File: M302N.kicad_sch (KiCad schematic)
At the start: 3 parts, among them J1 Analog, J2 Digital, U101 W5500

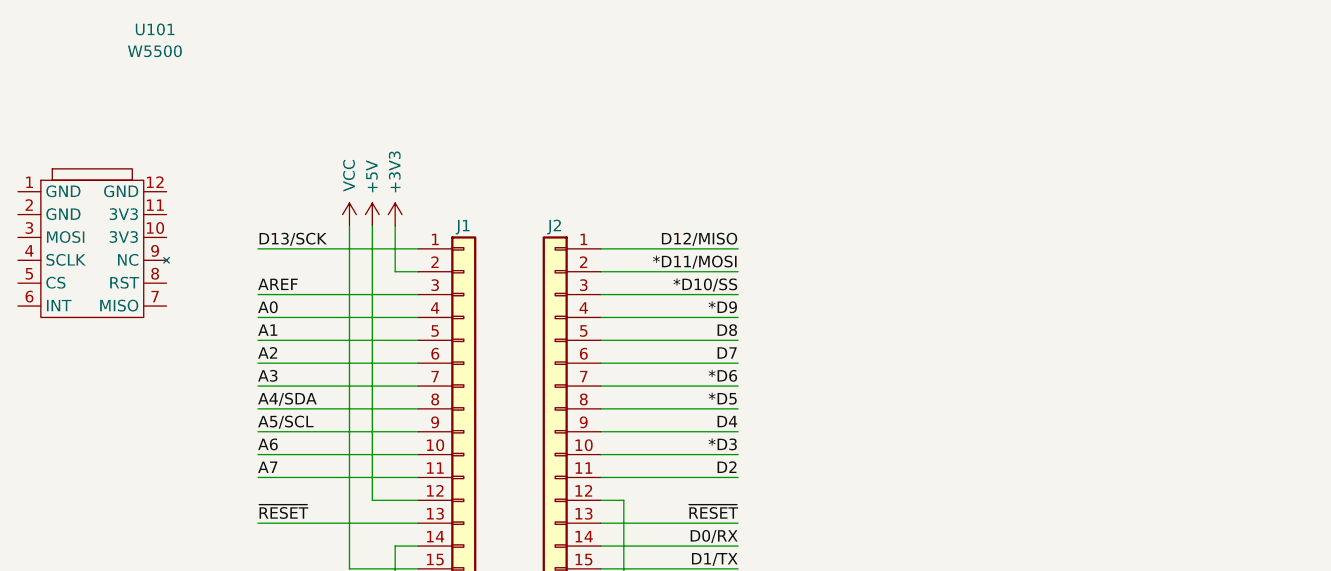
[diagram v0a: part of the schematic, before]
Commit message: W5500新しいシンボルとフットパターン
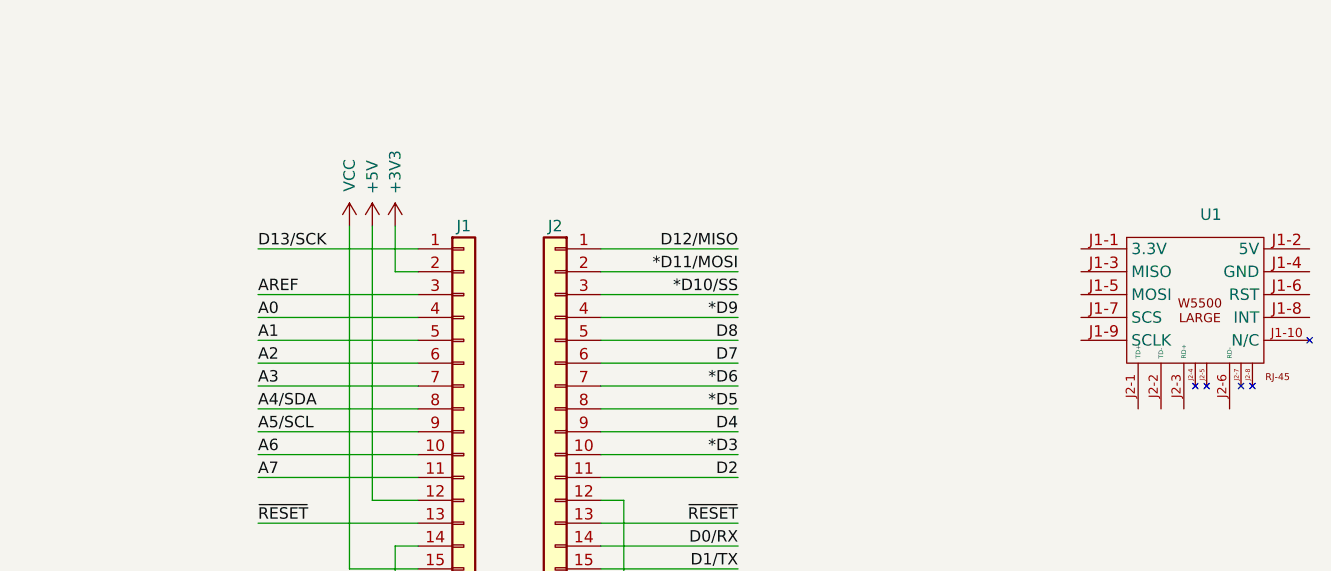
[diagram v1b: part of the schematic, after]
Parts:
- removed U101: W5500, symbol holly:W5500
- added U1: W5500, HOLLY2:W5500LARGE, symbol holly:W5500LARGE
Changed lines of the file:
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@@
 	(label "D4"
 		(at 154.94 88.9 180)
-		(fields_autoplaced yes)
 		(effects
 			(font
@@
 	(label "*D5"
 		(at 154.94 86.36 180)
-		(fields_autoplaced yes)
 		(effects
 			(font
@@
 	(label "A2"
 		(at 101.6 81.28 0)
-		(fields_autoplaced yes)
 		(effects
 			(font
@@
 	(label "D7"
 		(at 154.94 81.28 180)
-		(fields_autoplaced yes)
 		(effects
 			(font
@@
 	(label "D13{slash}SCK"
 		(at 101.6 68.58 0)
-		(fields_autoplaced yes)
 		(effects
 			(font
@@
 	(label "A7"
 		(at 101.6 93.98 0)
-		(fields_autoplaced yes)
 		(effects
 			(font
@@
 	(label "*D6"
 		(at 154.94 83.82 180)
-		(fields_autoplaced yes)
 		(effects
 			(font
@@
 	(label "*D11{slash}MOSI"
 		(at 154.94 71.12 180)
-		(fields_autoplaced yes)
 		(effects
 			(font
@@
 	(label "A1"
 		(at 101.6 78.74 0)
-		(fields_autoplaced yes)
 		(effects
 			(font
@@
 	(label "A4{slash}SDA"
 		(at 101.6 86.36 0)
-		(fields_autoplaced yes)
 		(effects
 			(font
@@
 	(label "A5{slash}SCL"
 		(at 101.6 88.9 0)
-		(fields_autoplaced yes)
 		(effects
 			(font
@@
 	(label "A3"
 		(at 101.6 83.82 0)
-		(fields_autoplaced yes)
 		(effects
 			(font
@@
 	(label "~{RESET}"
 		(at 154.94 99.06 180)
-		(fields_autoplaced yes)
 		(effects
 			(font
@@
 	(label "~{RESET}"
 		(at 101.6 99.06 0)
-		(fields_autoplaced yes)
 		(effects
 			(font
@@
 	(label "A6"
 		(at 101.6 91.44 0)
-		(fields_autoplaced yes)
 		(effects
 			(font
@@
 	(label "A0"
 		(at 101.6 76.2 0)
-		(fields_autoplaced yes)
 		(effects
 			(font
@@
 	(label "*D9"
 		(at 154.94 76.2 180)
-		(fields_autoplaced yes)
 		(effects
 			(font
@@
 	(label "*D3"
 		(at 154.94 91.44 180)
-		(fields_autoplaced yes)
 		(effects
 			(font
@@
 	(label "D2"
 		(at 154.94 93.98 180)
-		(fields_autoplaced yes)
 		(effects
 			(font
@@
 	(label "D8"
 		(at 154.94 78.74 180)
-		(fields_autoplaced yes)
 		(effects
 			(font
@@
 	(label "D1{slash}TX"
 		(at 154.94 104.14 180)
-		(fields_autoplaced yes)
 		(effects
 			(font
@@
 	(label "D0{slash}RX"
 		(at 154.94 101.6 180)
-		(fields_autoplaced yes)
 		(effects
 			(font
@@
 	(label "AREF"
 		(at 101.6 73.66 0)
-		(fields_autoplaced yes)
 		(effects
 			(font
@@
 	(label "*D10{slash}SS"
 		(at 154.94 73.66 180)
-		(fields_autoplaced yes)
 		(effects
 			(font
@@
 	(label "D12{slash}MISO"
 		(at 154.94 68.58 180)
-		(fields_autoplaced yes)
 		(effects
 			(font
@@
 	)
 	(symbol
-		(lib_id "holly:W5500")
-		(at 82.55 68.58 0)
-		(unit 1)
-		(exclude_from_sim no)
-		(in_bom yes)
-		(on_board yes)
-		(dnp no)
-		(fields_autoplaced yes)
-		(property "Reference" "U101"
-			(at 90.17 44.2425 0)
-			(effects
-				(font
-					(size 1.27 1.27)
-				)
-			)
-		)
-		(property "Value" "W5500"
-			(at 90.17 46.6668 0)
-			(effects
-				(font
-					(size 1.27 1.27)
-				)
-			)
-		)
-		(property "Footprint" ""
-			(at 82.55 68.58 0)
-			(effects
-				(font
-					(size 1.27 1.27)
-				)
-				(hide yes)
-			)
-		)
-		(property "Datasheet" ""
-			(at 81.28 78.74 0)
-			(effects
-				(font
-					(size 1.27 1.27)
-				)
-				(hide yes)
-			)
-		)
-		(property "Description" "Tzt smart electronics USR-ES1"
-			(at 82.55 68.58 0)
-			(effects
-				(font
-					(size 1.27 1.27)
-				)
-				(hide yes)
-			)
-		)
-		(pin "5"
-		)
-		(pin "7"
-		)
-		(pin "8"
-		)
-		(pin "1"
-		)
-		(pin "6"
-		)
-		(pin "10"
-		)
-		(pin "11"
-		)
-		(pin "12"
-		)
-		(pin "2"
-		)
-		(pin "3"
-		)
-		(pin "4"
-		)
-		(pin "9"
-		)
-		(instances
-			(project ""
-				(path "/0d35483a-0b12-46cc-b9f2-896fd6831779"
-					(reference "U101")
-					(unit 1)
-				)
-			)
-		)
-	)
-	(symbol
 		(lib_id "power:GND")
 		(at 142.24 106.68 0)
@@
 					(unit 1)
 				)
+			)
+		)
+	)
+	(symbol
+		(lib_id "holly:W5500LARGE")
+		(at 205.74 66.04 0)
+		(unit 1)
+		(exclude_from_sim no)
+		(in_bom yes)
+		(on_board yes)
+		(dnp no)
+		(fields_autoplaced yes)
+		(property "Reference" "U1"
+			(at 207.4697 64.77 0)
+			(effects
+				(font
+					(size 1.27 1.27)
+				)
+			)
+		)
+		(property "Value" "W5500"
+			(at 205.74 66.04 0)
+			(effects
+				(font
+					(size 1.27 1.27)
+				)
+				(hide yes)
+			)
+		)
+		(property "Footprint" "HOLLY2:W5500LARGE"
+			(at 205.74 66.04 0)
+			(effects
+				(font
+					(size 1.27 1.27)
+				)
+				(hide yes)
+			)
+		)
+		(property "Datasheet" ""
+			(at 205.74 66.04 0)
+			(effects
+				(font
+					(size 1.27 1.27)
+				)
+				(hide yes)
+			)
+		)
+		(property "Description" ""
+			(at 205.74 66.04 0)
+			(effects
+				(font
+					(size 1.27 1.27)
+				)
+				(hide yes)
+			)
+		)
+		(pin "J2-8"
+		)
+		(pin "J1-9"
+		)
+		(pin "J2-4"
+		)
+		(pin "J2-7"
+		)
+		(pin "J1-3"
+		)
+		(pin "J1-4"
+		)
+		(pin "J1-5"
+		)
+		(pin "J1-6"
+		)
+		(pin "J1-2"
+		)
+		(pin "J1-10"
+		)
+		(pin "J1-1"
+		)
+		(pin "J2-1"
+		)
+		(pin "J2-5"
+		)
+		(pin "J2-2"
+		)
+		(pin "J1-8"
+		)
+		(pin "J2-6"
+		)
+		(pin "J1-7"
+		)
+		(pin "J2-3"
+		)
+		(instances
+			(project ""
+				(path "/0d35483a-0b12-46cc-b9f2-896fd6831779"
+					(reference "U1")
+					(unit 1)
+				)

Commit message: 途中
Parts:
- added C101: 0.1uF, symbol Device:C_Small
- added D101: 1N4001, Diode_THT:D_DO-41_SOD81_P10.16mm_Horizontal, symbol Diode:1N4001
- added FL101: 0.1uF DDS1, HOLLY:DSS1, symbol 001-rescue:EMI_Filter_LCL-Device
- added J101: I2C-1, Connector_JST:JST_XH_S4B-XH-A_1x04_P2.50mm_Horizontal, symbol Connector_Generic:Conn_01x04
- added J102: I2C-2, Connector_JST:JST_XH_S4B-XH-A_1x04_P2.50mm_Horizontal, symbol Connector_Generic:Conn_01x04
- added J103: ADC_IN, Connector_JST:JST_XH_S3B-XH-A_1x03_P2.50mm_Horizontal, symbol Connector_Generic:Conn_01x03
- added J104: RJ45, symbol Connector:RJ45
- added J105: DC12V FAN, symbol Connector_Generic:Conn_01x02
- added R101: 10k, symbol Device:R_US
- added R102: TNR10V471K, symbol Device:R_Variable_US
- added SW101: SW_Reed, symbol Switch:SW_Reed
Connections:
- net *D10/SS: now also U1.J1-7 (SCS)
- net *D11/MOSI: now also U1.J1-5 (MOSI)
- net +5V: now also U1.J1-2 (5V), J101.2 (Pin_2), J102.2 (Pin_2), J103.3 (Pin_3), R101.1
- net A4/SDA: now also J101.3 (Pin_3), J102.3 (Pin_3)
- net A5/SCL: now also J101.4 (Pin_4), J102.4 (Pin_4)
- net A7: now also J103.2 (Pin_2)
- net D12/MISO: now also U1.J1-3 (MISO)
- net D13/SCK: now also U1.J1-9 (SCLK)
- net GND: now also U1.J1-4 (GND), C101.2, D101.2 (A), FL101.2, J101.1 (Pin_1), J102.1 (Pin_1), J103.1 (Pin_1), J104.7, J104.8, J105.1 (Pin_1), R102.2, SW101.1
- net ~{RESET}: now also U1.J1-6 (RST), R101.2, SW101.2
- net at U1.J2-1 (TD+): now also J104.1
- net at U1.J2-2 (TD-): now also J104.2
- net at U1.J2-3 (RD+): now also J104.3
- net at U1.J2-6 (RD-): now also J104.6
- new net +12V: C101.1, D101.1 (K), FL101.3, J104.4, J104.5, J105.2 (Pin_2), R102.1
- no-connect marks 0 -> 2
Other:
- note added: "NJU7223"
- company: (none) -> YS-Lab Masafumi Horimoto
- title: (none) -> M302N
- moved on the sheet: U1

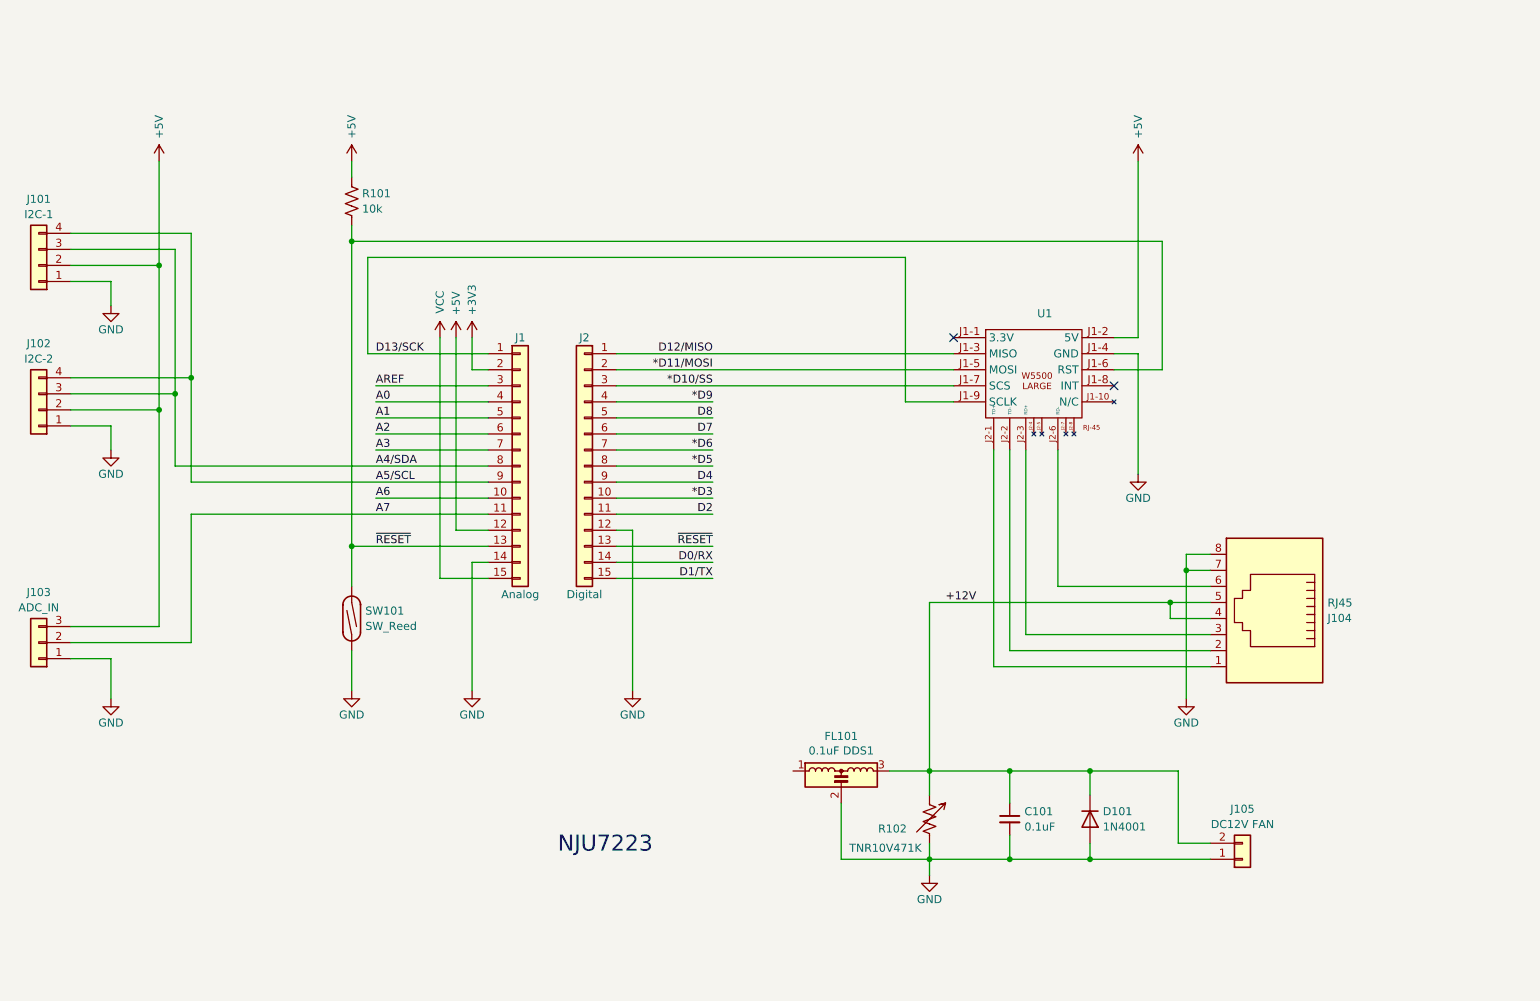
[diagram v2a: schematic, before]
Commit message: W5500との接続はソケット
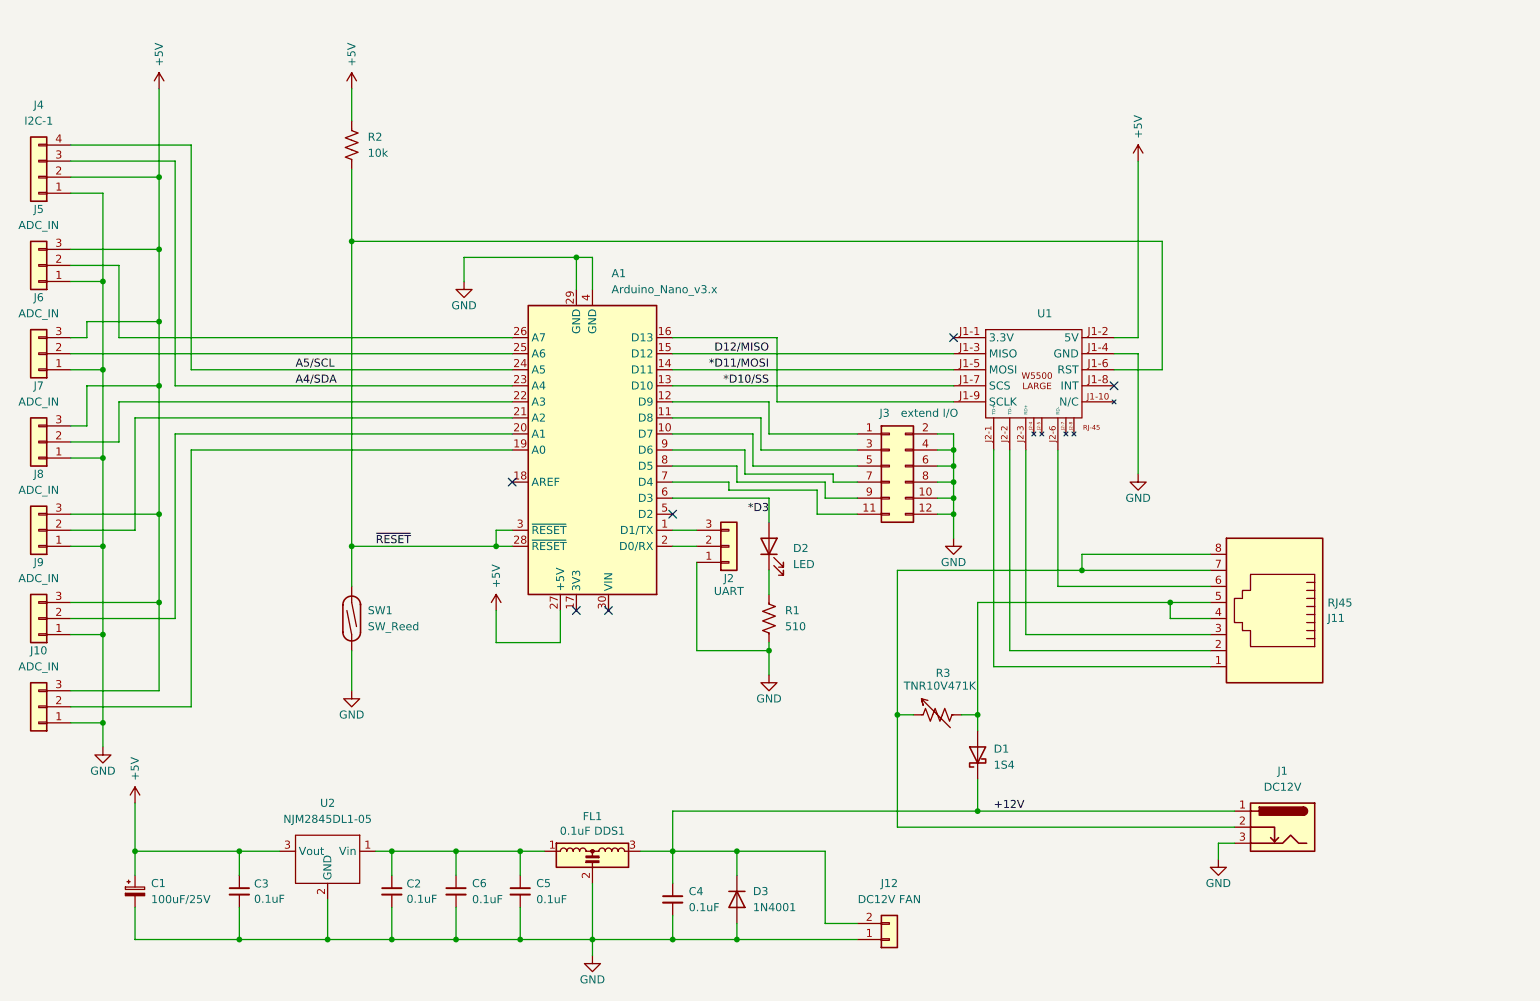
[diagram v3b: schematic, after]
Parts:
- removed J1: Analog, Connector_PinHeader_2.54mm:PinHeader_1x15_P2.54mm_Vertical, symbol Connector_Generic:Conn_01x15
- removed J102: I2C-2, Connector_JST:JST_XH_S4B-XH-A_1x04_P2.50mm_Horizontal, symbol Connector_Generic:Conn_01x04
- removed J2: Digital, Connector_PinHeader_2.54mm:PinHeader_1x15_P2.54mm_Vertical, symbol Connector_Generic:Conn_01x15
- added A1: Arduino_Nano_v3.x, Arduino:Arduino_Nano, symbol MCU_Module:Arduino_Nano_v3.x
- added C1: 100uF/25V, Capacitor_THT:C_Radial_D5.0mm_H11.0mm_P2.00mm, symbol Device:C_Polarized_Small
- added C2, C3, C5, C6: 0.1uF, Capacitor_THT:C_Disc_D4.3mm_W1.9mm_P5.00mm, symbol Device:C_Small
- added D1: 1S4, Resistor_THT:R_Axial_DIN0204_L3.6mm_D1.6mm_P5.08mm_Horizontal, symbol Device:D_Schottky
- added D2: LED, LED_THT:LED_D3.0mm, symbol Device:LED
- added J1: DC12V, Connector_BarrelJack:BarrelJack_GCT_DCJ200-10-A_Horizontal, symbol Connector:Barrel_Jack_Switch_Pin3Ring
- added J2: UART, Connector_PinHeader_2.54mm:PinHeader_1x03_P2.54mm_Vertical, symbol Connector_Generic:Conn_01x03
- added J3: extend I/O, Connector_PinHeader_2.54mm:PinHeader_2x06_P2.54mm_Vertical, symbol Connector_Generic:Conn_02x06_Odd_Even
- added J5, J6, J7, J8, J9: ADC_IN, Connector_JST:JST_XH_S3B-XH-A_1x03_P2.50mm_Horizontal, symbol Connector_Generic:Conn_01x03
- added R1: 510, Resistor_THT:R_Axial_DIN0207_L6.3mm_D2.5mm_P7.62mm_Horizontal, symbol Device:R_US
- added U2: NJM2845DL1-05, HOLLY2:NJM2845, symbol holly:NJM2845DL1
- C4: renamed from C101; footprint (none) -> Capacitor_THT:C_Disc_D4.3mm_W1.9mm_P5.00mm
- FL1: renamed from FL101; footprint HOLLY:DSS1 -> HOLLY2:DSS1
- J11: renamed from J104; footprint (none) -> HOLLY2:RJ45_Neltron_7810-8P8C
- J12: renamed from J105; footprint (none) -> Connector_JST:JST_XH_S2B-XH-A_1x02_P2.50mm_Horizontal
- R2: renamed from R101; footprint (none) -> Resistor_THT:R_Axial_DIN0207_L6.3mm_D2.5mm_P7.62mm_Horizontal
- renumbered D101 to D3, J103 to J10, J101 to J4, R102 to R3, SW101 to SW1
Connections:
- net *D10/SS: now also A1.13 (D10)
- net *D11/MOSI: now also A1.14 (D11)
- net *D3: now also A1.6 (D3), D2.2 (A)
- net +12V: now also D1.1 (K), J1.1; no longer J11.4, J11.5, R3.1
- net +5V: now also A1.27 (+5V), C1.1, C3.1, J5.3 (Pin_3), J6.3 (Pin_3), J7.3 (Pin_3), J8.3 (Pin_3), J9.3 (Pin_3), U2.3 (Vout)
- net A4/SDA: now also A1.23 (A4)
- net A5/SCL: now also A1.24 (A5)
- net D12/MISO: now also A1.15 (D12)
- net GND: now also A1.29 (GND), A1.4 (GND), C1.2, C2.2, C3.2, C5.2, C6.2, J1.3, J2.1 (Pin_1), J3.10 (Pin_10), J3.12 (Pin_12), J3.2 (Pin_2), J3.4 (Pin_4), J3.6 (Pin_6), J3.8 (Pin_8), J5.1 (Pin_1), J6.1 (Pin_1), J7.1 (Pin_1), J8.1 (Pin_1), J9.1 (Pin_1), R1.2, U2.2 (GND); no longer J11.7, J11.8, R3.2
- net ~{RESET}: now also A1.28 (~{RESET}), A1.3 (~{RESET})
- net at FL1.1: now also C2.1, C5.1, C6.1, U2.1 (Vin)
- net A7: no longer names the net of J10.2 (Pin_2)
- net A7: now also A1.19 (A0)
- net D13/SCK: no longer names the net of U1.J1-9 (SCLK)
- net D13/SCK: now also A1.16 (D13)
- new net: D2.1 (K), R1.1
- new net: D1.2 (A), J11.4, J11.5, R3.2
- new net: A1.26 (A7), J5.2 (Pin_2)
- new net: A1.22 (A3), J7.2 (Pin_2)
- new net: J1.2, J11.7, J11.8, R3.1
- new net: A1.2 (D0/RX), J2.2 (Pin_2)
- new net: A1.1 (D1/TX), J2.3 (Pin_3)
- new net: A1.12 (D9), J3.1 (Pin_1)
- new net: A1.7 (D4), J3.11 (Pin_11)
- new net: A1.11 (D8), J3.3 (Pin_3)
- new net: A1.10 (D7), J3.5 (Pin_5)
- new net: A1.9 (D6), J3.7 (Pin_7)
- new net: A1.8 (D5), J3.9 (Pin_9)
- new net: A1.25 (A6), J6.2 (Pin_2)
- new net: A1.21 (A2), J8.2 (Pin_2)
- new net: A1.20 (A1), J9.2 (Pin_2)
- no-connect marks 2 -> 6
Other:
- note removed: "NJU7223"
- moved on the sheet: C4, D3, FL1, J10, J12, J4, R2, R3

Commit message: PCB設計途中
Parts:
- added J13, J14: Conn_01x05_Socket, Connector_PinSocket_2.54mm:PinSocket_1x05_P2.54mm_Vertical, symbol Connector:Conn_01x05_Socket
- added J15, J16: Conn_01x05_Pin, symbol Connector:Conn_01x05_Pin
- added J17: Conn_01x08_Pin, symbol Connector:Conn_01x08_Pin
- added J18, J19: Conn_01x04_Socket, Connector_PinSocket_2.54mm:PinSocket_1x04_P2.54mm_Vertical, symbol Connector:Conn_01x04_Socket
- A1: footprint Arduino:Arduino_Nano -> Module:Arduino_Nano
- SW1: footprint (none) -> HOLLY:REED_SW
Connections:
- net *D10/SS: no longer A1.13 (D10), U1.J1-7 (SCS)
- net *D11/MOSI: no longer A1.14 (D11), U1.J1-5 (MOSI)
- net +5V: now also J14.1 (Pin_1); no longer U1.J1-2 (5V)
- net D12/MISO: no longer A1.15 (D12), U1.J1-3 (MISO)
- net GND: now also J14.2 (Pin_2); no longer U1.J1-4 (GND)
- net ~{RESET}: now also J14.3 (Pin_3); no longer U1.J1-6 (RST)
- net at U1.J2-1 (TD+): now also J17.1 (Pin_1); no longer J11.1
- net at U1.J2-2 (TD-): now also J17.2 (Pin_2); no longer J11.2
- net at U1.J2-3 (RD+): now also J17.3 (Pin_3); no longer J11.3
- net at U1.J2-6 (RD-): now also J17.6 (Pin_6); no longer J11.6
- net at A1.16 (D13): now also J13.5 (Pin_5); no longer U1.J1-9 (SCLK)
- new net: A1.15 (D12), J13.2 (Pin_2)
- new net: A1.14 (D11), J13.3 (Pin_3)
- new net: A1.13 (D10), J13.4 (Pin_4)
- new net: J16.1 (Pin_1), U1.J1-2 (5V)
- new net: J16.2 (Pin_2), U1.J1-4 (GND)
- new net: J16.3 (Pin_3), U1.J1-6 (RST)
- new net: J11.6, J19.2 (Pin_2)
- new net: J11.1, J18.1 (Pin_1)
- new net: J11.2, J18.2 (Pin_2)
- new net: J11.3, J18.3 (Pin_3)
- new net: J15.2 (Pin_2), U1.J1-3 (MISO)
- new net: J15.3 (Pin_3), U1.J1-5 (MOSI)
- new net: J15.4 (Pin_4), U1.J1-7 (SCS)
- new net: J15.5 (Pin_5), U1.J1-9 (SCLK)
- no-connect marks 6 -> 20
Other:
- moved on the sheet: J11, U1

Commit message: PCB設計とRJ45モジュラー
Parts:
- J10, J6, J7, J8, J9: footprint Connector_JST:JST_XH_S3B-XH-A_1x03_P2.50mm_Horizontal -> Connector_JST:JST_XH_B3B-XH-A_1x03_P2.50mm_Vertical
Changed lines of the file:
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@@
 			)
 		)
-		(property "Footprint" "Connector_JST:JST_XH_S3B-XH-A_1x03_P2.50mm_Horizontal"
+		(property "Footprint" "Connector_JST:JST_XH_B3B-XH-A_1x03_P2.50mm_Vertical"
 			(at 48.26 82.55 0)
 			(effects
@@
 			)
 		)
-		(property "Footprint" "Connector_JST:JST_XH_S3B-XH-A_1x03_P2.50mm_Horizontal"
+		(property "Footprint" "Connector_JST:JST_XH_B3B-XH-A_1x03_P2.50mm_Vertical"
 			(at 48.26 124.46 0)
 			(effects
@@
 			)
 		)
-		(property "Footprint" "Connector_JST:JST_XH_S3B-XH-A_1x03_P2.50mm_Horizontal"
+		(property "Footprint" "Connector_JST:JST_XH_B3B-XH-A_1x03_P2.50mm_Vertical"
 			(at 48.26 68.58 0)
 			(effects
@@
 			)
 		)
-		(property "Footprint" "Connector_JST:JST_XH_S3B-XH-A_1x03_P2.50mm_Horizontal"
+		(property "Footprint" "Connector_JST:JST_XH_B3B-XH-A_1x03_P2.50mm_Vertical"
 			(at 48.26 96.52 0)
 			(effects
@@
 			)
 		)
-		(property "Footprint" "Connector_JST:JST_XH_S3B-XH-A_1x03_P2.50mm_Horizontal"
+		(property "Footprint" "Connector_JST:JST_XH_B3B-XH-A_1x03_P2.50mm_Vertical"
 			(at 48.26 110.49 0)
 			(effects
